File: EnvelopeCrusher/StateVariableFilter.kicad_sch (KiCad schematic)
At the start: 17 parts, among them U3 TL072, U4 TL072

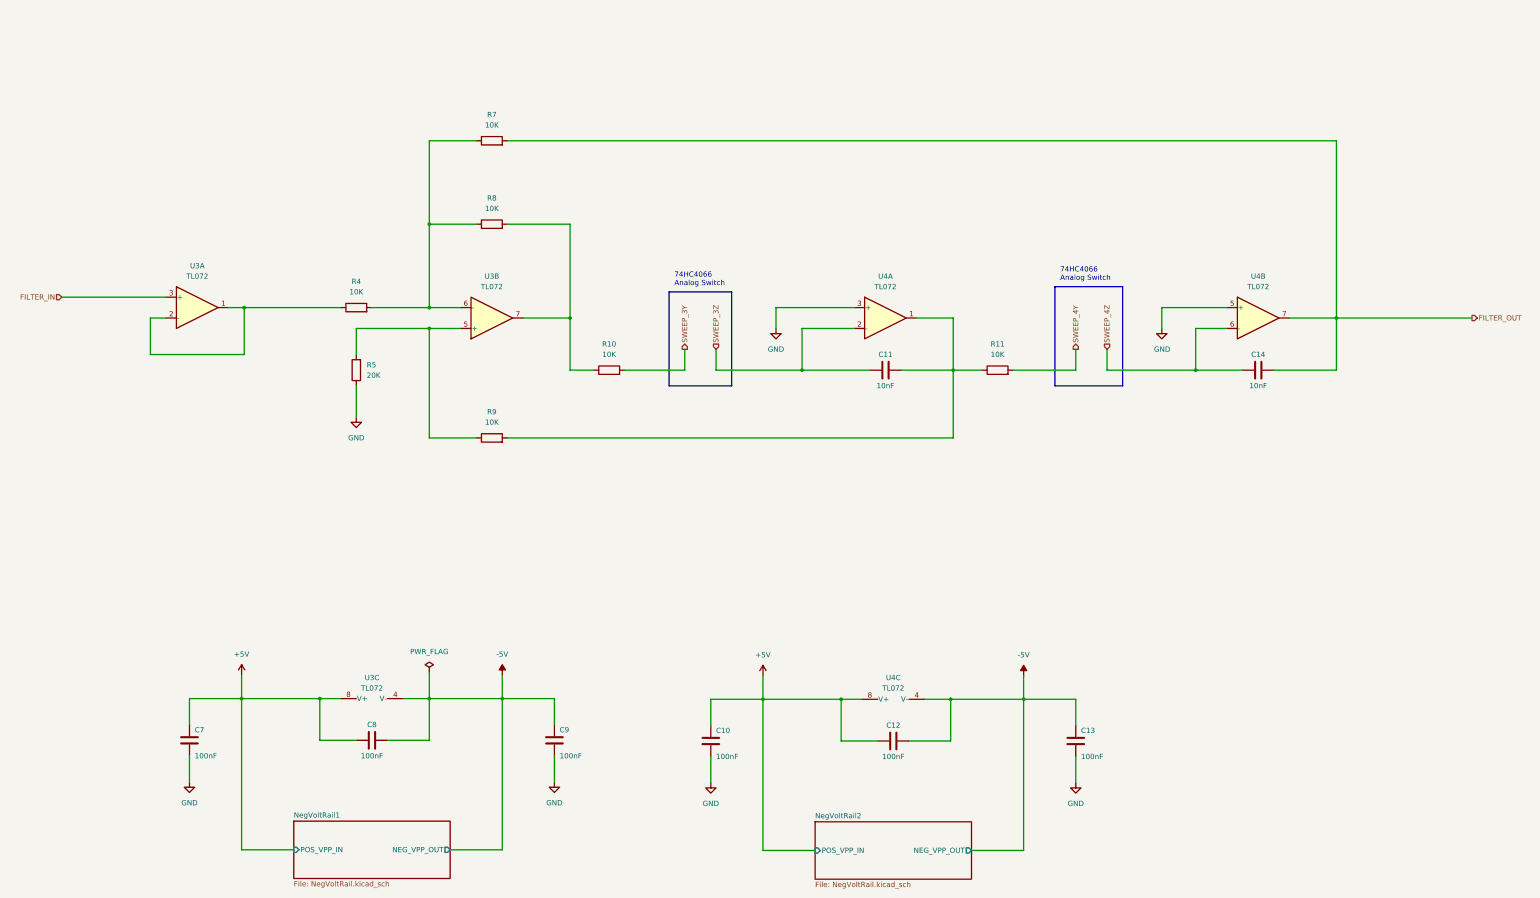
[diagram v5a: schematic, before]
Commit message: updated schematic
- Added values and comments to state-variable filter block
- Updated footprints
- Changed Dual Op Amp: TL072 to AM358
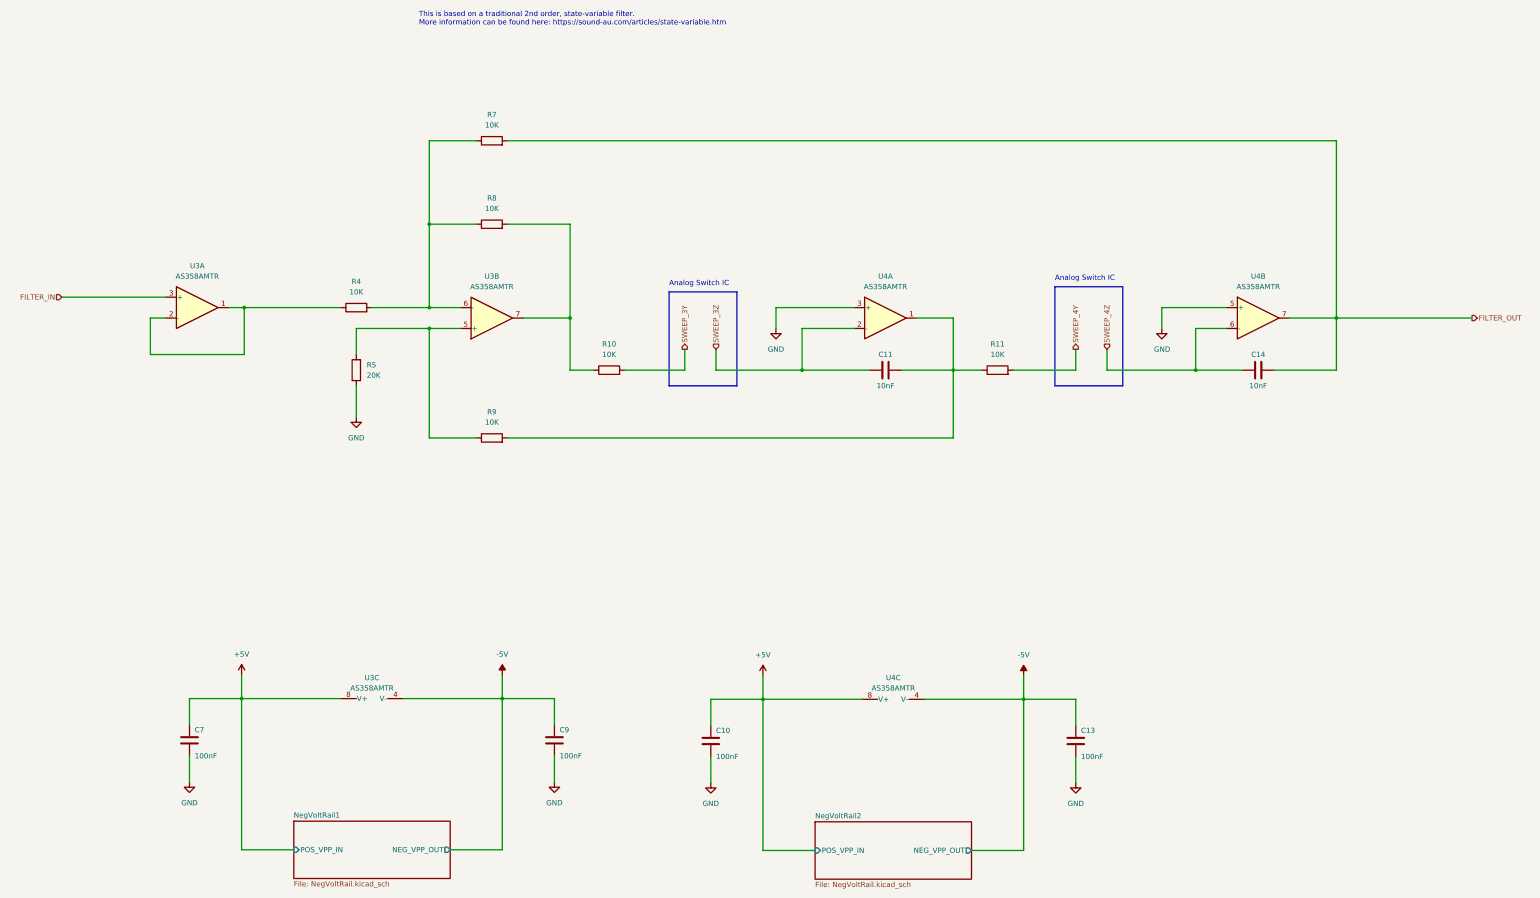
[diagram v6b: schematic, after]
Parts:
- removed C12, C8: 100nF, Capacitor_SMD:C_0805_2012Metric_Pad1.18x1.45mm_HandSolder, symbol Device:C
- U3, U4: value TL072 -> AS358AMTR; footprint (none) -> Package_SO:SOIC-8_3.9x4.9mm_P1.27mm
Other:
- note added: "Analog Switch IC"
- note added: "This is based on a traditional 2nd order, state-variable filter. More information can be found here: https://sound-au.com/articles/state-variable.htm"
- note removed: "74HC4066 Analog Switch"

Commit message: organised layout into functional blocks
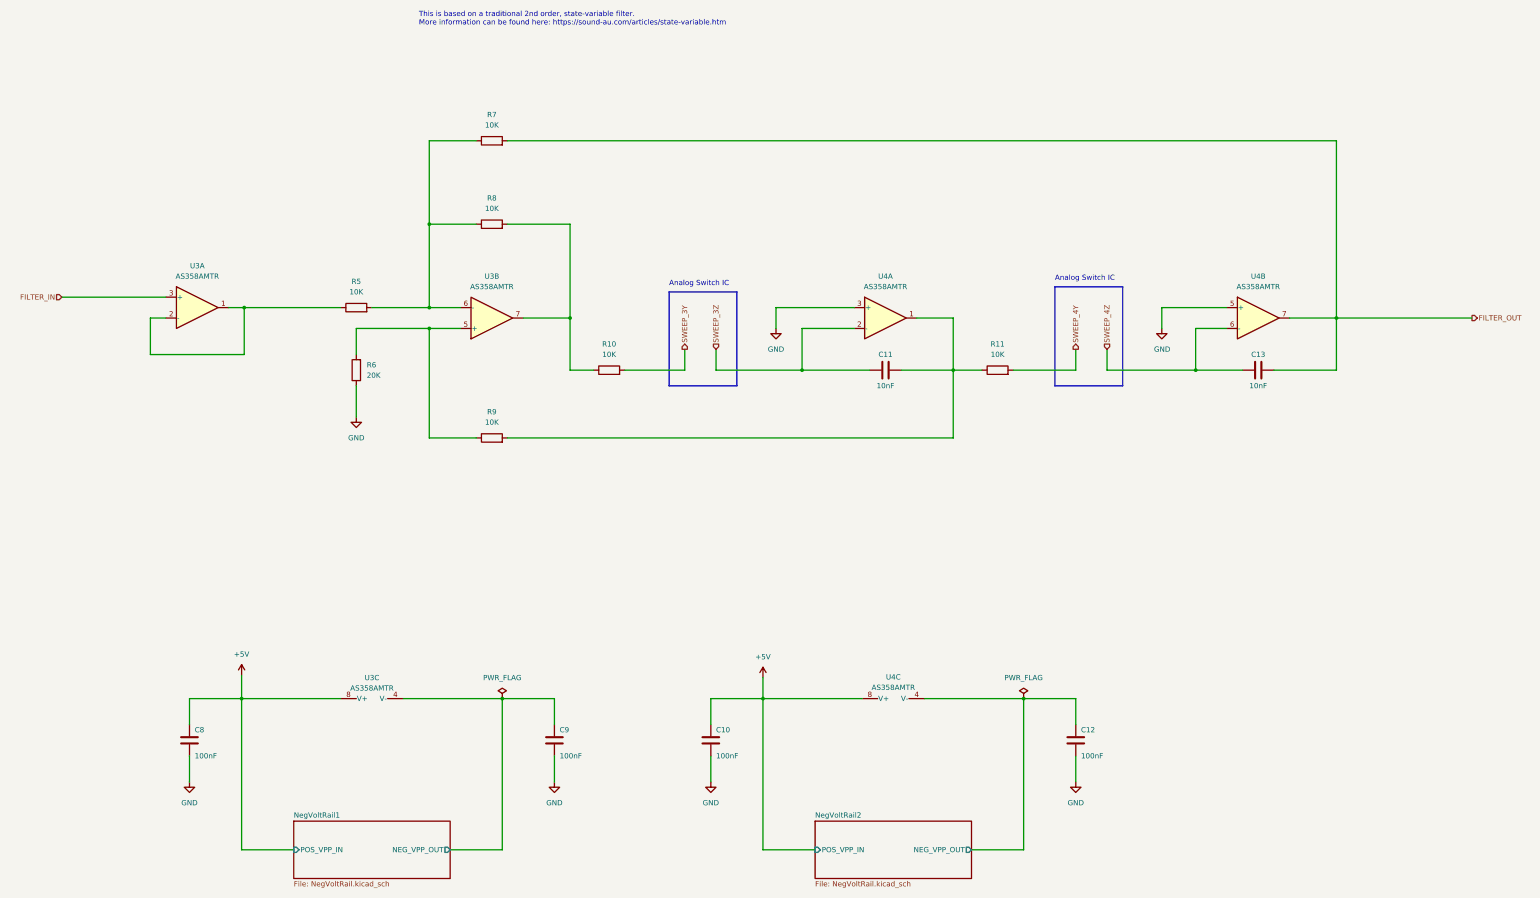
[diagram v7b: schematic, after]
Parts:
- renumbered C13 to C12, C14 to C13, C7 to C8, R4 to R5, R5 to R6
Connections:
- net -5V renamed NegVoltRail1/NEG_VPP_OUT
- net NegVoltRail1/NEG_VPP_OUT: no longer C12.2, U4.4 (V-)
- new net NegVoltRail2/NEG_VPP_OUT: C12.2, U4.4 (V-)
